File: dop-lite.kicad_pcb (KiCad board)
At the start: 4 copper layers, 50 x 50 mm, 25 parts, among them J1 Power Input, J2 Power Output, Q1 IRF7319, Q2 NMOS 40V×5A Vgsth<3, SW1 ON/OFF button, U1 IP2721_PHY, U2 LM2574N−12G_PHY

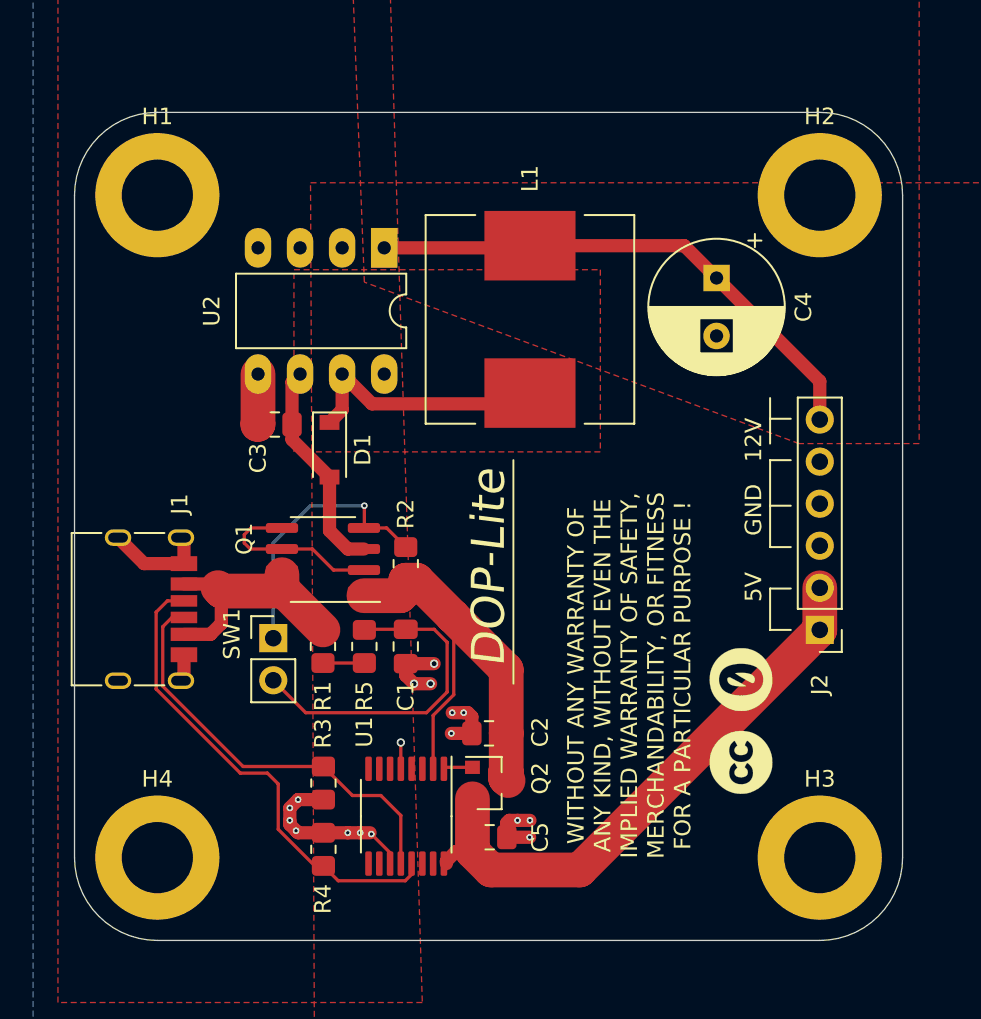
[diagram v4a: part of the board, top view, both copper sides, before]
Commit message: Resolves #1 : Use M2.5 mounting hole
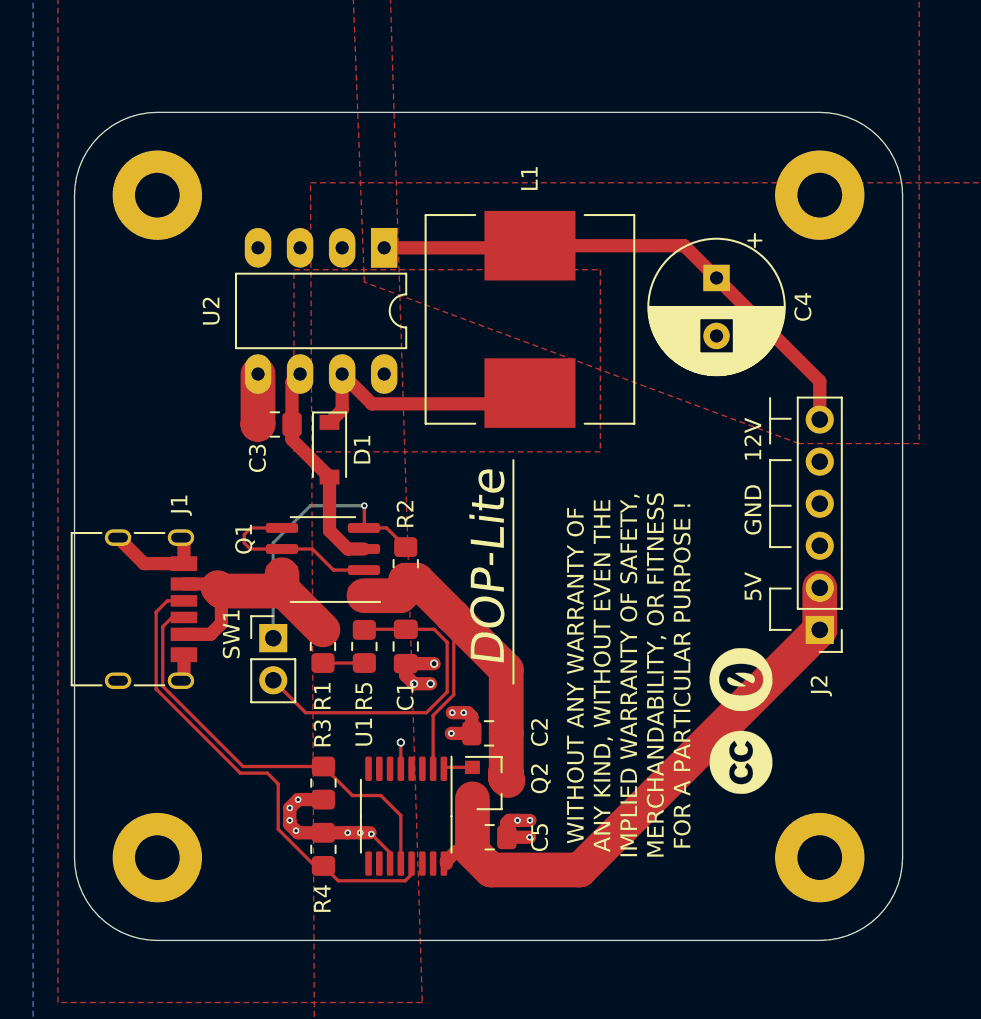
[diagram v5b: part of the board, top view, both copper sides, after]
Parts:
- H1, H2, H3, H4: value M4 -> M2.5; footprint MountingHole:MountingHole_4.3mm_M4_DIN965_Pad -> MountingHole:MountingHole_2.7mm_M2.5_Pad

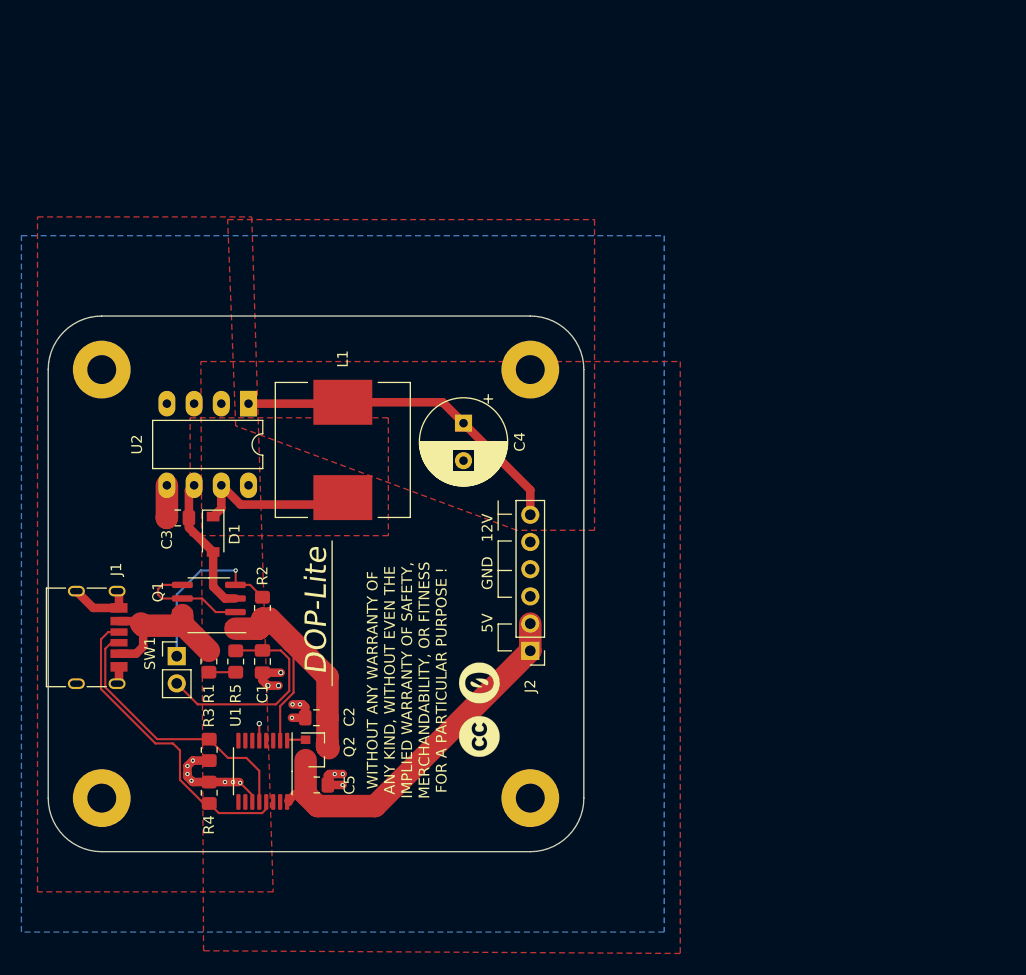
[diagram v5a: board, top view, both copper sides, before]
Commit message: rotate pcb to be legible without bending the neck
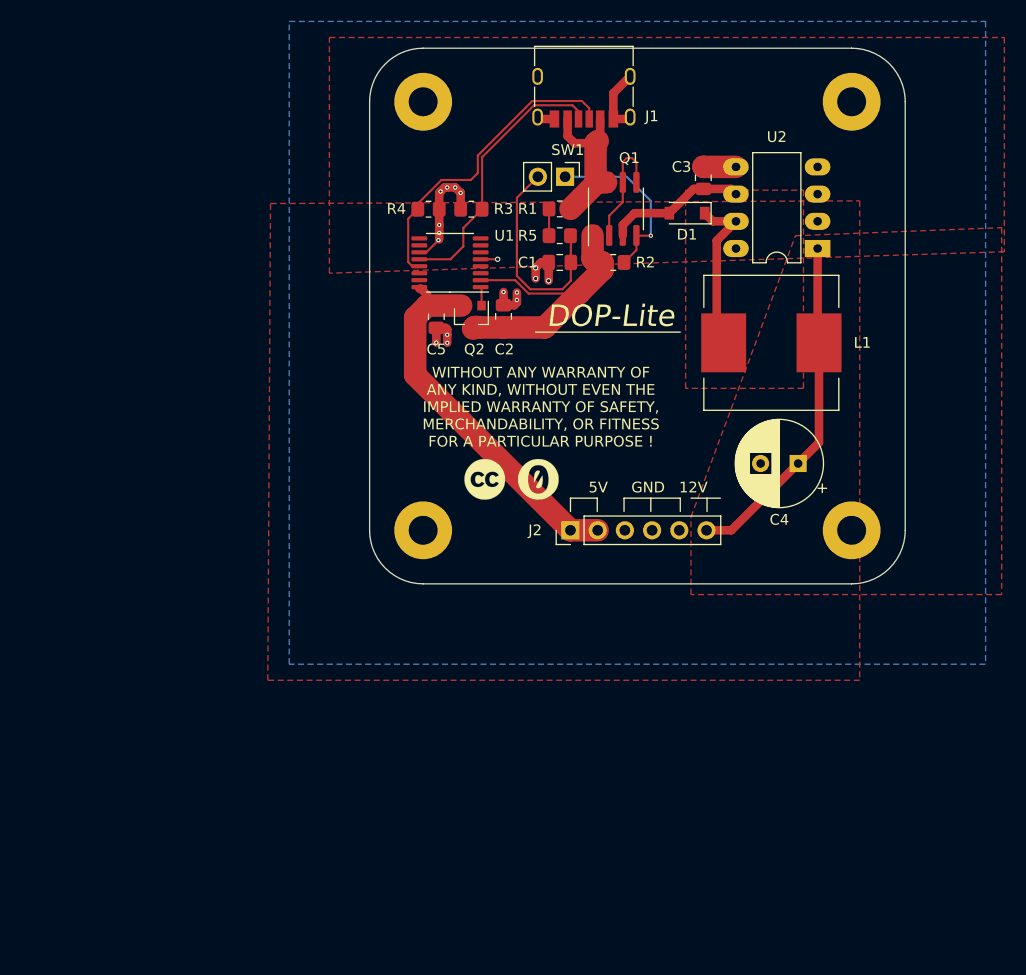
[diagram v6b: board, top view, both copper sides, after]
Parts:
- moved H1 74.3 mm to (125.0, 105.0), turned to 270 degrees
- moved H4 71.6 mm to (85.0, 105.0), turned to 270 degrees
- moved J1 70.6 mm to (100.0, 102.6), turned to 180 degrees
- moved C3 58.4 mm to (111.2, 112.1), turned to 270 degrees
- moved R4 58.2 mm to (85.5, 115.0), turned to 0 degrees
- moved SW1 57.6 mm to (98.2, 112.0), turned to 270 degrees
- moved R3 56.1 mm to (89.5, 115.0), turned to 180 degrees
- moved U2 55.1 mm to (121.8, 118.7), turned to 180 degrees
- moved R1 53.5 mm to (97.8, 115.0), turned to 180 degrees
- moved D1 53.4 mm to (109.6, 115.4), turned to 180 degrees
- moved Q1 53.0 mm to (103.0, 115.0), turned to 90 degrees
- moved U1 50.6 mm to (87.5, 120.0), turned to 180 degrees
- moved R5 50.0 mm to (97.8, 117.5), turned to 0 degrees
- moved C1 46.5 mm to (97.8, 120.0), turned to 180 degrees
- moved R2 46.0 mm to (102.8, 120.0), turned to 0 degrees
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
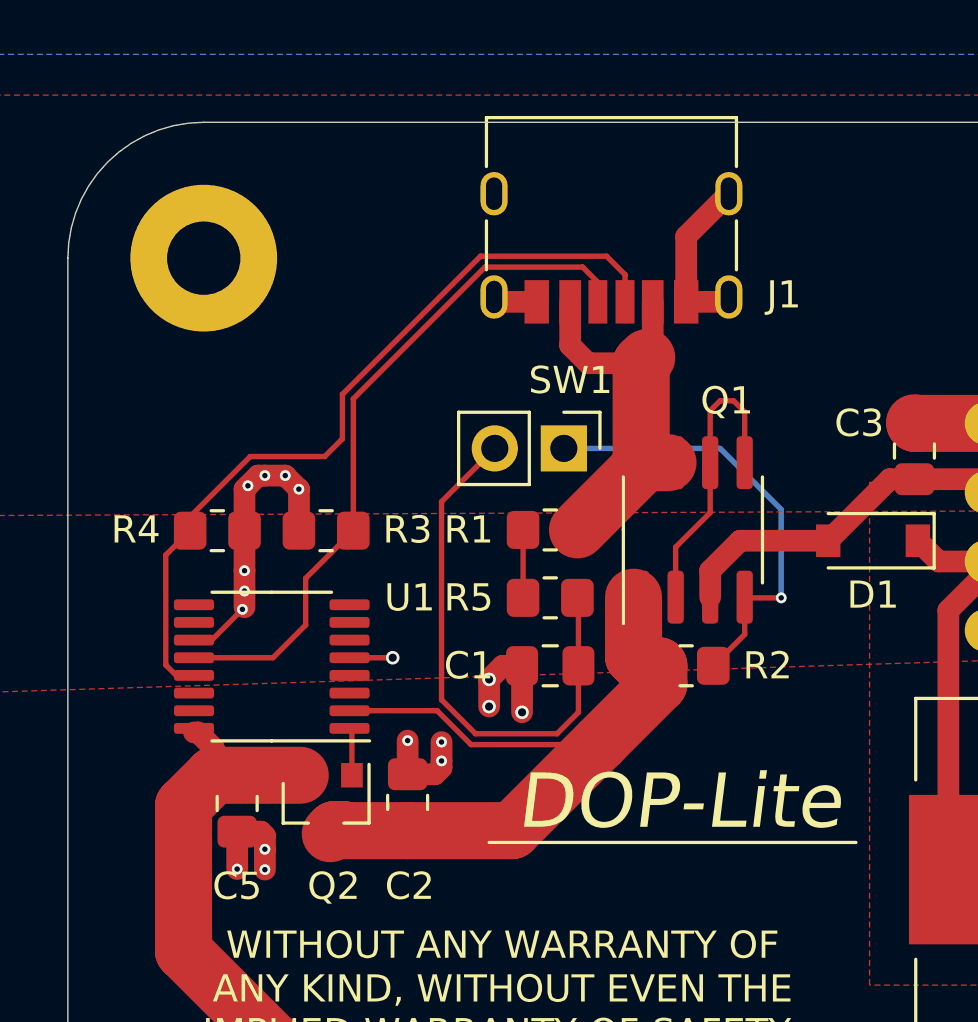
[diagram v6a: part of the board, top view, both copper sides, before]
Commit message: Resolves #2 : Move the usb receptacle 1~1.25 mm to the outer edge ; add some measurements
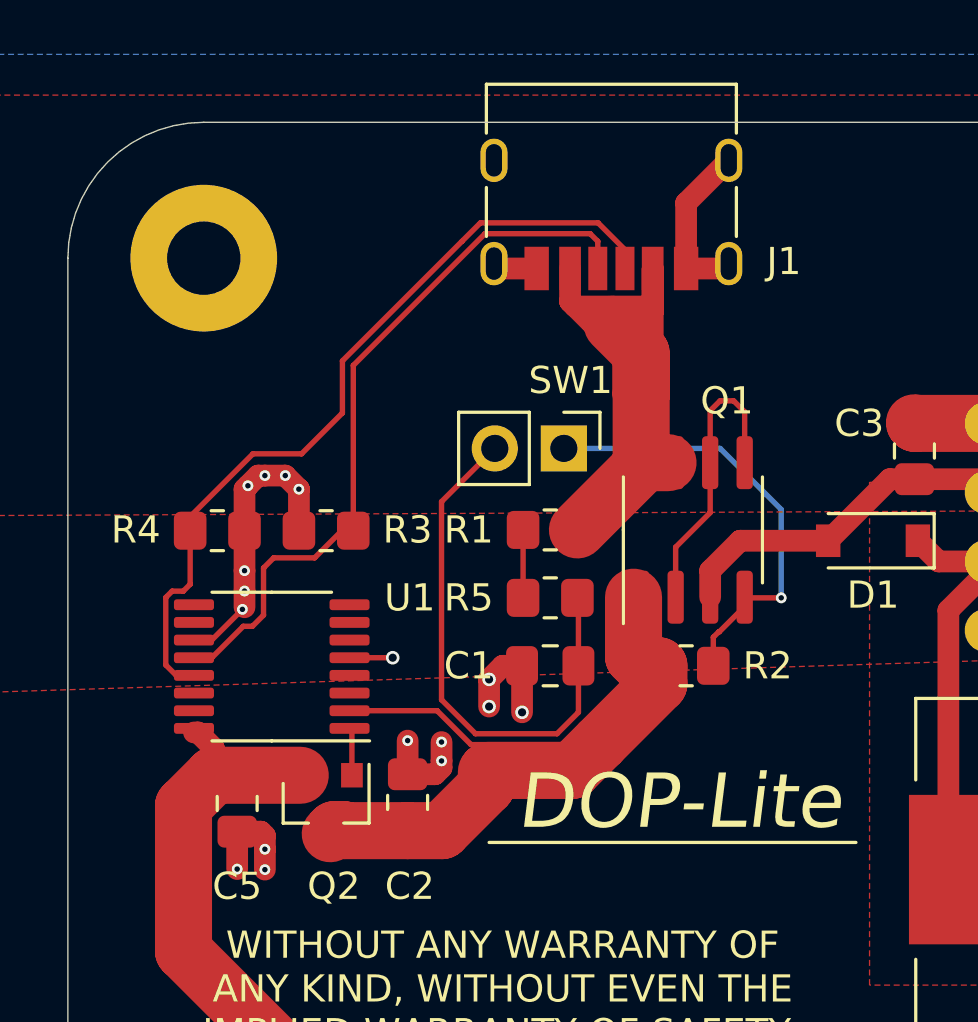
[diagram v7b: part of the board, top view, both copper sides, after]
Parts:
- moved J1 1.23 mm to (100.0, 101.4)
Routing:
- net Net-(J1-PadA9): track 15.3 -> 25.6 mm
- net /CC2: track 25.6 -> 27.0 mm
